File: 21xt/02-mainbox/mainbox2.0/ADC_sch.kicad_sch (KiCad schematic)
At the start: 14 parts, among them J6 Conn_01x06, U1 AD7175-2BRUZ

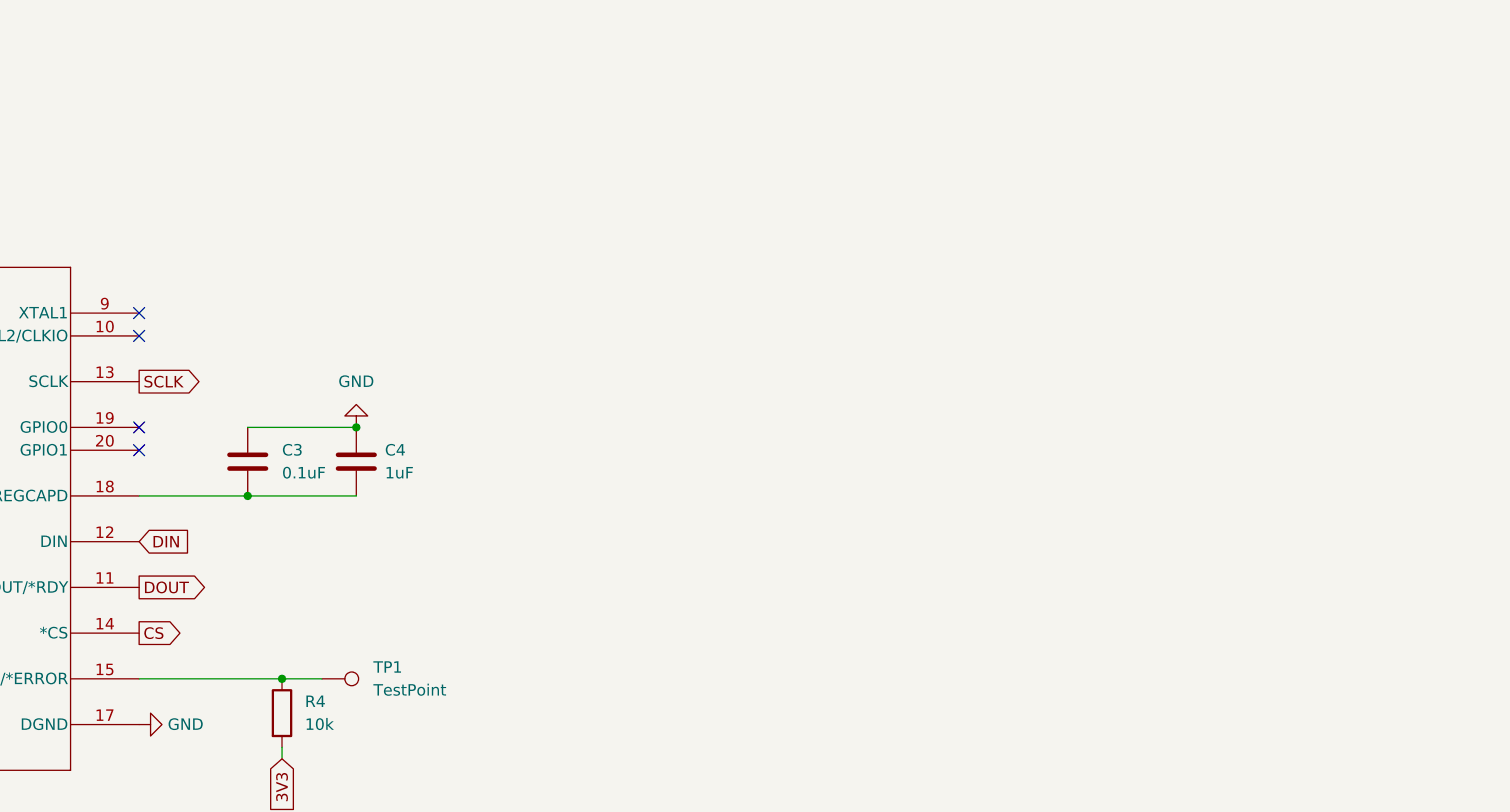
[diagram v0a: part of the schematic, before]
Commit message: schematic markups minus pcie
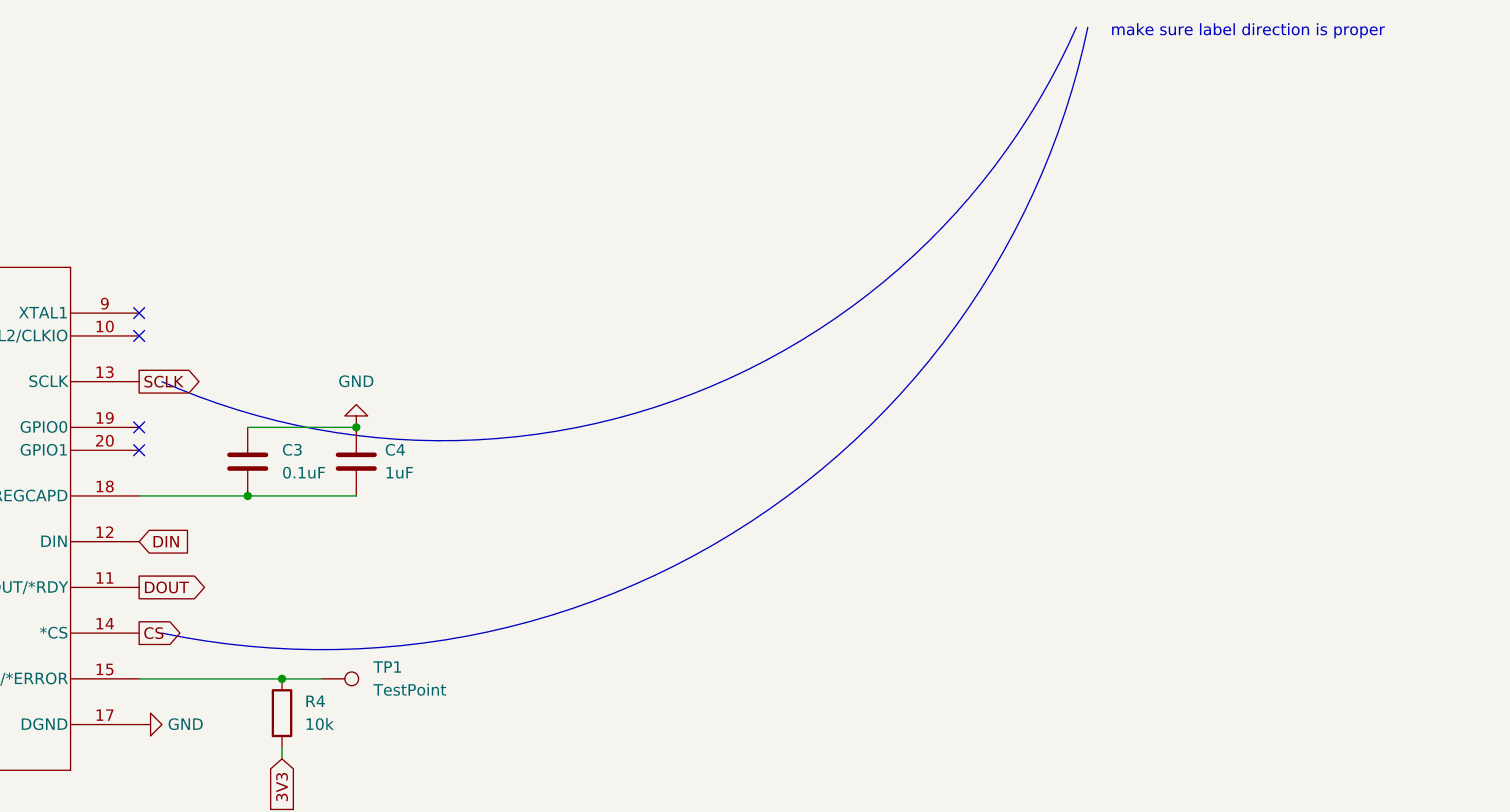
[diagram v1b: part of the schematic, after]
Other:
- note added: "make sure label direction is proper"
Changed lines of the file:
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@@
     (stroke (width 0) (type default))
+  )
+  (arc (start 317.5 44.45) (mid 274.8538 85.1771) (end 215.9 83.82)
+    (stroke (width 0) (type default))
+    (fill (type none))
+  )
+  (arc (start 318.77 44.45) (mid 281.2754 99.4101) (end 215.9 111.76)
+    (stroke (width 0) (type default))
+    (fill (type none))
   )
   (text "NOTE FOR REFOUT:On power-up, if the internal reference is not being used, \nwrite to the ADC mode register, disabling the internal reference. \nThis is controlled by the REF_EN bit (Bit 15) in the ADC mode register"
@@
     (effects (font (size 1.27 1.27)) (justify left bottom))
   )
+  (text "make sure label direction is proper" (at 321.31 45.72 0)
+    (effects (font (size 1.27 1.27)) (justify left bottom))
+  )

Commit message: progress
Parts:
- removed J6: Conn_01x06, symbol Connector_Generic:Conn_01x06
- removed R4: 10k, symbol Device:R
- removed TP1: TestPoint, symbol Connector:TestPoint
- added C11, C12, C13, C38: 0.1uF, Capacitor_SMD:C_0603_1608Metric, symbol Device:C
- added IC4, IC5: SN74LVC2T45DCTTG4, 21xt_footprints:SOP65P400X130-8N, symbol Logic_LevelTranslator:SN74LVC2T45DCTTG4
- added J2: Conn_01x10, 21xt_footprints:908160010(picolex-10), symbol Connector_Generic:Conn_01x10
- C1, C2, C3, C4, C5, C6, C8: footprint (none) -> Capacitor_SMD:C_0603_1608Metric
- C10: value C -> 0.1uF; footprint (none) -> Capacitor_SMD:C_0603_1608Metric
- C7: value 0.1 -> 0.1uF; footprint (none) -> Capacitor_SMD:C_0603_1608Metric
- C9: value C -> 10uF; footprint (none) -> Capacitor_SMD:C_0603_1608Metric
- U1: footprint (none) -> 21xt_footprints:RU_24_ADI
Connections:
- net 3V3: now also C12.2, C38.2, IC4.1 (VCCA), IC5.1 (VCCA)
- net 5VADC/SENSOR: now also J2.6 (Pin_6)
- net ANI1: now also J2.1 (Pin_1)
- net ANI2: now also J2.2 (Pin_2)
- net ANI3: now also J2.3 (Pin_3)
- net ANI4: now also J2.4 (Pin_4)
- net GND: now also U1.15 (*SYNC/*ERROR), C11.1, C12.1, C13.1, C38.1, IC4.4 (GND), IC4.5 (DIR), IC5.4 (GND), IC5.5 (DIR), J2.5 (Pin_5)
- net CS renamed RPi_SPI_CS
- net DIN renamed ADC_SPI_DIN
- net DOUT renamed ADC_SPI_DOUT
- new net 5.2V: C11.2, C13.2, IC4.8 (VCCB), IC5.8 (VCCB)
- new net DIGITAL_INPUT_1: IC4.7 (B1), J2.7 (Pin_7)
- new net DIGITAL_INPUT_2: IC4.6 (B2), J2.8 (Pin_8)
- new net DIGITAL_INPUT_3: IC5.7 (B1), J2.9 (Pin_9)
- new net DIGITAL_INPUT_4: IC5.6 (B2), J2.10 (Pin_10)
- new net DIGITAL_OUTPUT_1: IC4.2 (A1)
- new net DIGITAL_OUTPUT_2: IC4.3 (A2)
- new net DIGITAL_OUTPUT_3: IC5.2 (A1)
- new net DIGITAL_OUTPUT_4: IC5.3 (A2)
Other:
- note added: "AGND"
- note added: "DGND"
- note added: "may need more signal isolation"
- note removed: "make sure label direction is proper"
- moved on the sheet: C1, C10, C2, C3, C4, C5, C6, C7, C8, C9, U1
